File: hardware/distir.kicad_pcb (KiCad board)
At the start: 2 copper layers, 18.9 x 44.6 mm, 14 parts, among them K1 S3B-PH-SM4, P1 CON-SENSOR, U1 M24C64, U2 DRILL, U3 DRILL

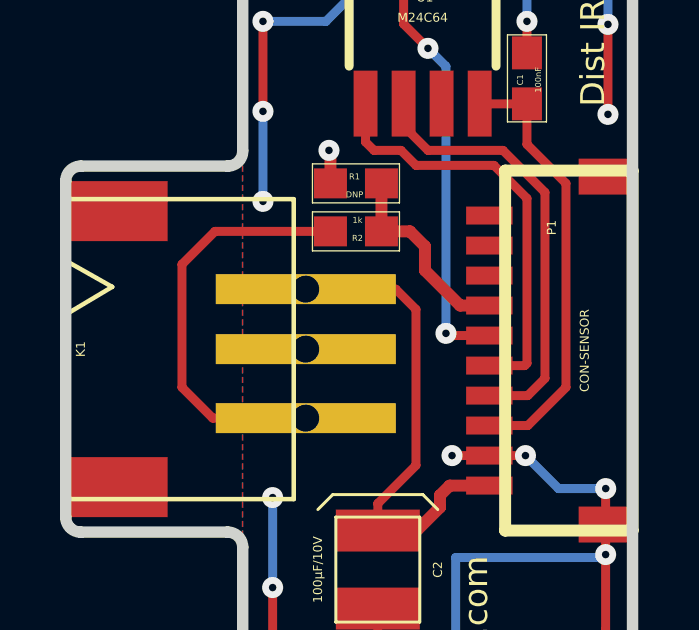
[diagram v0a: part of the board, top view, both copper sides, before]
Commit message: switch to smd connector
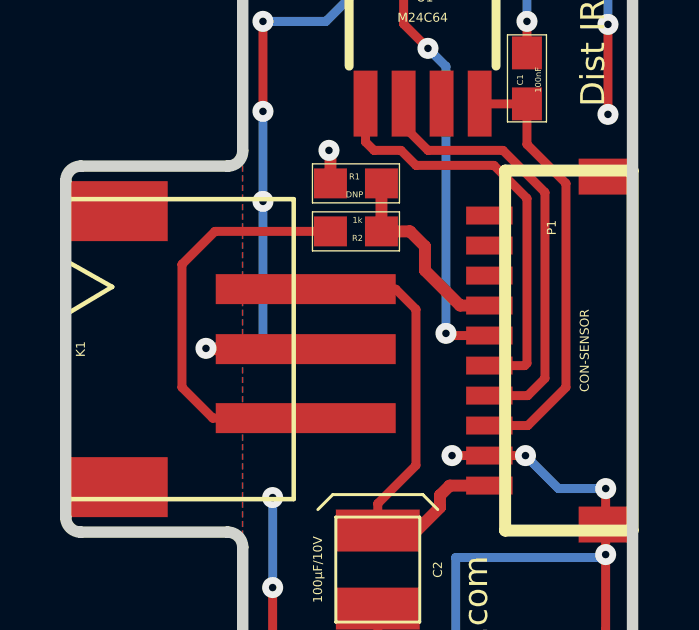
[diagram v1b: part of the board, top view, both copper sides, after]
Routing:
- net GND: track 81.6 -> 91.5 mm, vias 26 -> 27
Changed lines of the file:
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@@
     (links 19)
     (no_connects 0)
-    (area 131.834499 79.469877 151.109681 124.474544)
+    (area 131.00184 79.469877 281.44724 163.01974)
     (thickness 1.6002)
     (drawings 25)
-    (tracks 129)
+    (tracks 135)
     (zones 0)
     (modules 14)
@@
       (effects (font (size 0.3 0.3) (thickness 0.075)))
     )
-    (fp_text value S3B-PH-SM4 (at 0 -0.5 90) (layer F.Fab)
+    (fp_text value S3B-PH-SM4 (at -0.175 1.875 90) (layer F.Fab)
       (effects (font (size 0.3 0.3) (thickness 0.075)))
     )
@@
     (pad "" smd rect (at -4.6 1.7 90) (size 2 3.4) (layers Vorderseite F.Paste F.Mask))
     (pad "" smd rect (at 4.6 1.7 90) (size 2 3.4) (layers Vorderseite F.Paste F.Mask))
-    (pad 3 thru_hole rect (at -2.3 8 90) (size 1 6) (drill 0.9) (layers *.Cu *.Mask F.Paste F.SilkS)
+    (pad 3 smd rect (at -2.3 8 90) (size 1 6) (layers Vorderseite F.Paste F.Mask)
       (net 8 "Net-(K1-Pad3)"))
-    (pad 2 thru_hole rect (at 0 8 90) (size 1 6) (drill 0.9) (layers *.Cu *.Mask F.Paste F.SilkS)
+    (pad 2 smd rect (at 0 8 90) (size 1 6) (layers Vorderseite F.Paste F.Mask)
       (net 1 GND))
-    (pad 1 thru_hole rect (at 2 8 90) (size 1 6) (drill 0.9) (layers *.Cu *.Mask F.Paste F.SilkS)
+    (pad 1 smd rect (at 2 8 90) (size 1 6) (layers Vorderseite F.Paste F.Mask)
       (net 6 "Net-(C2-Pad1)"))
   )
@@
     (effects (font (size 0.8 0.8) (thickness 0.14986)))
   )
+  (segment (start 138.6 97) (end 138.6 101.5) (width 0.29972) (layer Rückseite) (net 1))
+  (segment (start 142 89.7) (end 140.7 91) (width 0.29972) (layer Rückseite) (net 1))
+  (segment (start 140.7 91) (end 138.6 91) (width 0.29972) (layer Rückseite) (net 1))
+  (via (at 138.6 91) (size 0.70104) (drill 0.24892) (layers Vorderseite Rückseite) (net 1))
+  (segment (start 138.6 91) (end 138.6 94) (width 0.29972) (layer Vorderseite) (net 1))
+  (via (at 138.6 94) (size 0.70104) (drill 0.24892) (layers Vorderseite Rückseite) (net 1))
+  (segment (start 138.6 94) (end 138.6 97) (width 0.29972) (layer Rückseite) (net 1))
+  (via (at 138.6 97) (size 0.70104) (drill 0.24892) (layers Vorderseite Rückseite) (net 1))
+  (segment (start 142 89.5) (end 142 89.7) (width 0.29972) (layer Rückseite) (net 1))
+  (segment (start 136.725 101.925) (end 140.025 101.925) (width 0.39878) (layer Vorderseite) (net 1))
+  (segment (start 136.7 101.9) (end 136.725 101.925) (width 0.29972) (layer Vorderseite) (net 1))
+  (via (at 136.7 101.9) (size 0.70104) (drill 0.24892) (layers Vorderseite Rückseite) (net 1))
+  (segment (start 138.2 101.9) (end 136.7 101.9) (width 0.39878) (layer Rückseite) (net 1))
+  (segment (start 138.6 101.5) (end 138.2 101.9) (width 0.29972) (layer Rückseite) (net 1))
   (segment (start 147.4 91) (end 147.4 87.9) (width 0.29972) (layer Rückseite) (net 1))
   (via (at 147.4 91) (size 0.70104) (drill 0.24892) (layers Vorderseite Rückseite) (net 1))
@@
   (via (at 147.3 87.8) (size 0.70104) (drill 0.24892) (layers Vorderseite Rückseite) (net 1))
   (segment (start 147.4 87.9) (end 147.3 87.8) (width 0.29972) (layer Rückseite) (net 1))
-  (segment (start 142 89.5) (end 142 89.7) (width 0.29972) (layer Rückseite) (net 1))
-  (via (at 138.6 97) (size 0.70104) (drill 0.24892) (layers Vorderseite Rückseite) (net 1))
-  (segment (start 138.6 94) (end 138.6 97) (width 0.29972) (layer Rückseite) (net 1))
-  (via (at 138.6 94) (size 0.70104) (drill 0.24892) (layers Vorderseite Rückseite) (net 1))
-  (segment (start 138.6 91) (end 138.6 94) (width 0.29972) (layer Vorderseite) (net 1))
-  (via (at 138.6 91) (size 0.70104) (drill 0.24892) (layers Vorderseite Rückseite) (net 1))
-  (segment (start 140.7 91) (end 138.6 91) (width 0.29972) (layer Rückseite) (net 1))
-  (segment (start 142 89.7) (end 140.7 91) (width 0.29972) (layer Rückseite) (net 1))
   (segment (start 145.82394 88.00592) (end 145.82394 89.42394) (width 0.29972) (layer Vorderseite) (net 1))
   (via (at 145.9 89.5) (size 0.70104) (drill 0.24892) (layers Vorderseite Rückseite) (net 1))

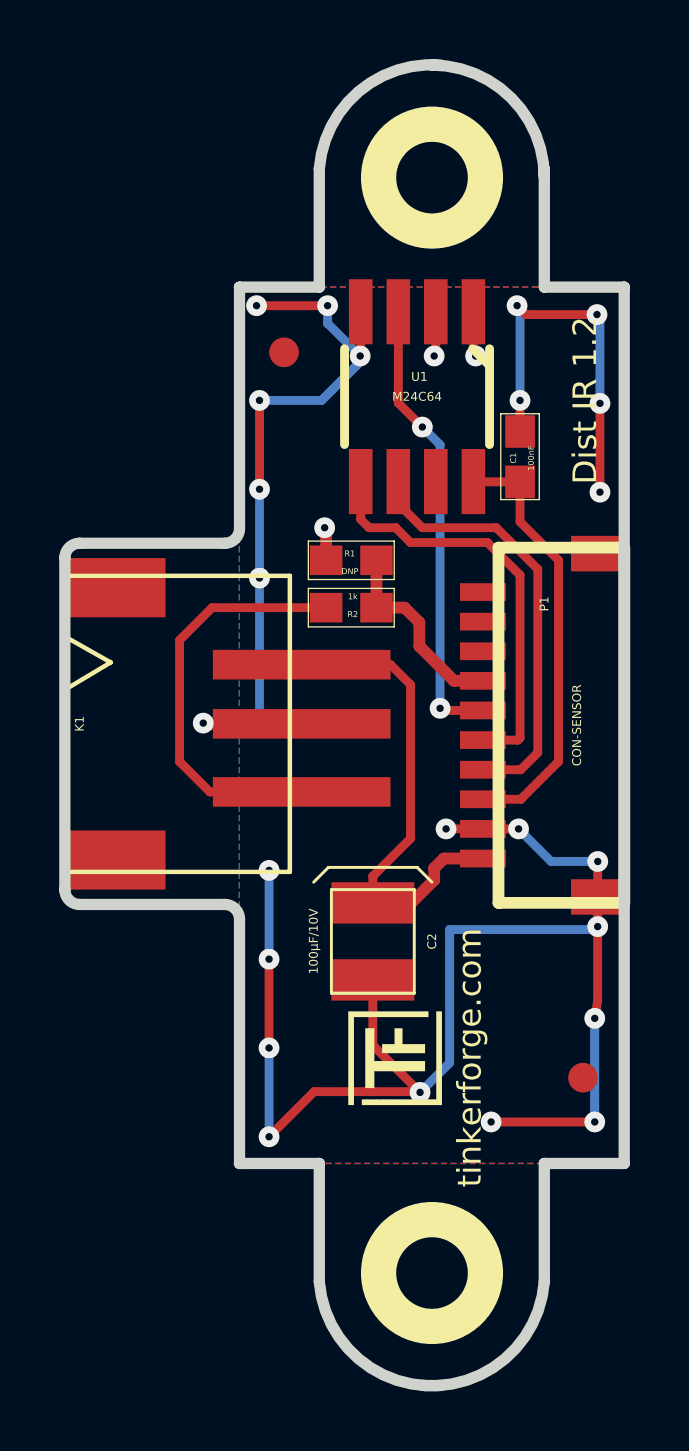
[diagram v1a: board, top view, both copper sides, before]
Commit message: fix edge cuts: set on grid
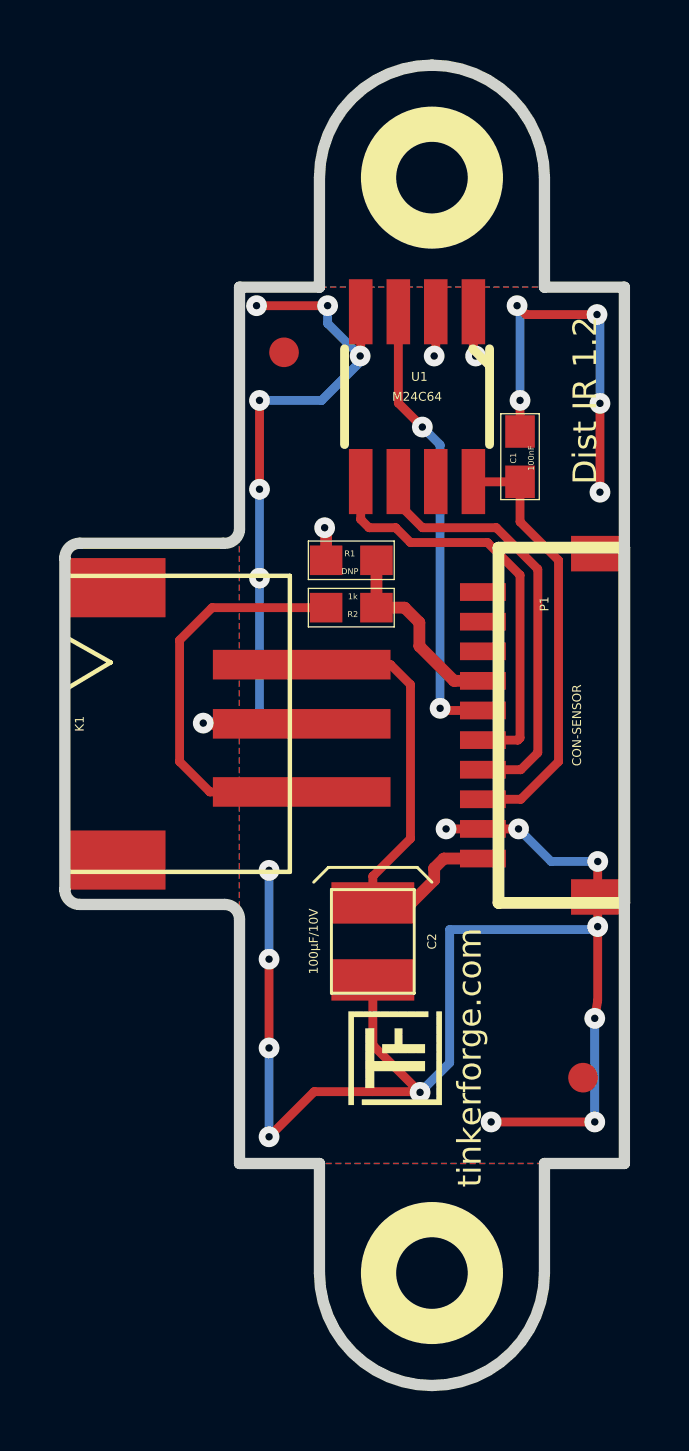
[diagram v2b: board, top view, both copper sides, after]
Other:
- outline, holes or cut-outs redrawn
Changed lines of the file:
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@@
-(kicad_pcb (version 4) (host pcbnew 4.0.2-4+6225~38~ubuntu15.10.1-stable)
+(kicad_pcb (version 4) (host pcbnew 4.0.7-e2-6376~58~ubuntu17.04.1)
   (general
     (links 19)
     (no_connects 0)
-    (area 131.00184 79.469877 281.44724 163.01974)
+    (area 131.834499 79.484499 151.115501 124.465501)
     (thickness 1.6002)
     (drawings 25)
@@
     (pad_drill 1.3)
     (pad_to_mask_clearance 0)
-    (aux_axis_origin 137.92708 124.27458)
+    (aux_axis_origin 144.425 120.475)
+    (grid_origin 144.425 120.475)
     (visible_elements FFFFFFBF)
     (pcbplotparams
@@
   )
   (module DRILL_NP (layer Vorderseite)
-    (at 144.42694 120.47474)
+    (at 144.425 120.475)
     (fp_text reference U2 (at 0 0) (layer F.SilkS) hide
       (effects (font (size 0.29972 0.29972) (thickness 0.0762)))
@@
   )
   (module DRILL_NP (layer Vorderseite)
-    (at 144.42694 83.47456)
+    (at 144.425 83.475)
     (fp_text reference U3 (at 0 0) (layer F.SilkS) hide
       (effects (font (size 0.29972 0.29972) (thickness 0.0762)))
@@
   )
   (gr_line (start 137.925 116.775) (end 137.925 108.525) (angle 90) (layer Edge.Cuts) (width 0.381))
-  (gr_line (start 137.925 95.3) (end 137.925 87.175) (angle 90) (layer Edge.Cuts) (width 0.381))
-  (gr_line (start 132.525 95.825) (end 137.425 95.825) (angle 90) (layer Edge.Cuts) (width 0.381))
-  (gr_line (start 137.425 108.025) (end 132.525 108.025) (angle 90) (layer Edge.Cuts) (width 0.381))
   (gr_arc (start 137.425 108.525) (end 137.425 108.025) (angle 90) (layer Edge.Cuts) (width 0.381))
-  (gr_arc (start 137.425 95.325) (end 137.925 95.325) (angle 90) (layer Edge.Cuts) (width 0.381))
+  (gr_line (start 137.425 108.025) (end 132.525 108.025) (angle 90) (layer Edge.Cuts) (width 0.381))
+  (gr_line (start 137.375 95.825) (end 132.525 95.825) (angle 90) (layer Edge.Cuts) (width 0.381))
+  (gr_arc (start 137.425 95.325) (end 137.925 95.375) (angle 90) (layer Edge.Cuts) (width 0.381))
+  (gr_line (start 140.625 120.475) (end 140.625 116.775) (angle 90) (layer Edge.Cuts) (width 0.381))
+  (gr_line (start 137.925 87.175) (end 137.925 95.375) (angle 90) (layer Edge.Cuts) (width 0.381))
+  (gr_line (start 140.625 87.175) (end 137.925 87.175) (angle 90) (layer Edge.Cuts) (width 0.381))
+  (gr_line (start 140.625 83.475) (end 140.625 87.175) (angle 90) (layer Edge.Cuts) (width 0.381))
+  (gr_line (start 148.225 87.175) (end 148.225 83.475) (angle 90) (layer Edge.Cuts) (width 0.381))
+  (gr_line (start 150.925 87.175) (end 148.225 87.175) (angle 90) (layer Edge.Cuts) (width 0.381))
+  (gr_line (start 150.925 116.775) (end 150.925 87.175) (angle 90) (layer Edge.Cuts) (width 0.381))
+  (gr_line (start 148.225 116.775) (end 150.925 116.775) (angle 90) (layer Edge.Cuts) (width 0.381))
+  (gr_line (start 148.225 120.475) (end 148.225 116.775) (angle 90) (layer Edge.Cuts) (width 0.381))
+  (gr_arc (start 144.425 120.475) (end 144.425 124.275) (angle 90) (layer Edge.Cuts) (width 0.381))
+  (gr_arc (start 144.425 120.475) (end 148.225 120.475) (angle 90) (layer Edge.Cuts) (width 0.381))
+  (gr_arc (start 144.425 83.475) (end 144.425 79.675) (angle 90) (layer Edge.Cuts) (width 0.381))
+  (gr_arc (start 144.425 83.475) (end 140.625 83.475) (angle 90) (layer Edge.Cuts) (width 0.381))
+  (gr_line (start 137.925 116.775) (end 140.625 116.775) (angle 90) (layer Edge.Cuts) (width 0.381))
   (gr_arc (start 132.525 96.325) (end 132.025 96.325) (angle 90) (layer Edge.Cuts) (width 0.381))
   (gr_arc (start 132.525 107.525) (end 132.525 108.025) (angle 90) (layer Edge.Cuts) (width 0.381))
@@
     (effects (font (size 0.8001 0.8001) (thickness 0.14986)))
   )
-  (gr_line (start 148.21916 87.1728) (end 150.91918 87.1728) (angle 90) (layer Edge.Cuts) (width 0.381))
-  (gr_line (start 137.91946 87.1728) (end 140.61948 87.1728) (angle 90) (layer Edge.Cuts) (width 0.381))
-  (gr_line (start 137.91946 116.77396) (end 140.61948 116.77396) (angle 90) (layer Edge.Cuts) (width 0.381))
-  (gr_line (start 148.21916 116.77396) (end 150.91918 116.77396) (angle 90) (layer Edge.Cuts) (width 0.381))
-  (gr_arc (start 144.41932 120.4722) (end 144.72158 124.27204) (angle 90) (layer Edge.Cuts) (width 0.381))
-  (gr_arc (start 144.41932 120.4722) (end 148.21916 120.77192) (angle 90) (layer Edge.Cuts) (width 0.381))
-  (gr_line (start 140.61948 120.77192) (end 140.61948 116.77142) (angle 90) (layer Edge.Cuts) (width 0.381))
-  (gr_line (start 148.21916 120.77192) (end 148.21916 116.77142) (angle 90) (layer Edge.Cuts) (width 0.381))
-  (gr_line (start 150.91918 116.77396) (end 150.91918 87.1728) (angle 90) (layer Edge.Cuts) (width 0.381))
-  (gr_arc (start 144.41932 83.47202) (end 144.41932 79.67218) (angle 90) (layer Edge.Cuts) (width 0.381))
-  (gr_arc (start 144.41932 83.47202) (end 140.61948 83.1723) (angle 90) (layer Edge.Cuts) (width 0.381))
-  (gr_line (start 148.21916 87.1728) (end 148.21916 83.1723) (angle 90) (layer Edge.Cuts) (width 0.381))
-  (gr_line (start 140.61948 87.1728) (end 140.61948 83.1723) (angle 90) (layer Edge.Cuts) (width 0.381))
   (gr_text "Dist IR 1.2" (at 149.6 91 90) (layer F.SilkS)
     (effects (font (size 0.8 0.8) (thickness 0.14986)))
@@
   (segment (start 135.9 103.2) (end 135.9 99.1) (width 0.29972) (layer Vorderseite) (net 8))
   (segment (start 136.925 104.225) (end 135.9 103.2) (width 0.29972) (layer Vorderseite) (net 8))
-  (zone (net 1) (net_name GND) (layer Vorderseite) (hatch edge 0.508)
+  (zone (net 1) (net_name GND) (layer Rückseite) (hatch edge 0.508)
     (connect_pads (clearance 0.24892))
     (min_thickness 0.24892)
@@
     )
   )
-  (zone (net 1) (net_name GND) (layer Rückseite) (hatch edge 0.508)
+  (zone (net 1) (net_name GND) (layer Vorderseite) (hatch edge 0.508)
     (connect_pads (clearance 0.24892))
     (min_thickness 0.24892)

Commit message: Add 3d information (final)
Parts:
- C1: footprint kicad-libraries:0603E -> kicad-libraries:C0603E
- C2: footprint 3528-21 -> kicad-libraries:3528-21
- Fiducial_Mark (x2): footprint Fiducial_Mark -> kicad-libraries:Fiducial_Mark
- P1: footprint CON-SENSOR -> kicad-libraries:CON-SENSOR
- R1, R2: footprint kicad-libraries:0603E -> kicad-libraries:R0603E
- Ref**: footprint Logo_31x31 -> kicad-libraries:Logo_31x31
- U2, U3: footprint DRILL_NP -> kicad-libraries:DRILL_NP
- VAL: footprint CE_5mm -> kicad-libraries:CE_5mm
- VAL: footprint WEEE_7mm -> kicad-libraries:WEEE_7mm
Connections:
- P1 pad 10: (no net) -> Net-(P1-Pad10)
- P1 pad 8: (no net) -> Net-(P1-Pad8)
- P1 pad 9: (no net) -> Net-(P1-Pad9)
- U1 pad 7: (no net) -> Net-(U1-Pad7)
